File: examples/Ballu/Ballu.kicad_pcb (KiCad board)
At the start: 4 copper layers, 32.4 x 45.2 mm, 82 parts, among them J1 COM-15111, J2 B2B-PH-K, J4 AFC01-S30FCA-00, J5 PinHeader2.54 1x3, J6 PinHeader2.54 1x3, J7 B2B-PH-K, Q1 20V 3.1A 860mW 112m?@4.5V,2.8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, Q2 60V 115mA 200mW 7.5?@10V,500m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, Q3 30V 4A 44m?@10V,4.3A 1.4W 1.3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, SW1 SKRHABE010, SW2 5.1mm switch, U1 LDL1117S33R, U2 MCP73831T-2ACI/OT, U3 ESP32-S3-WROOM-1-N16R8, U4 PESD5V0X1BT, U5 LSM6DS3TR-C, U6 QMC5883L, U7 ER-OLED-0.96-1.1, U8 MAX98357AETE+T

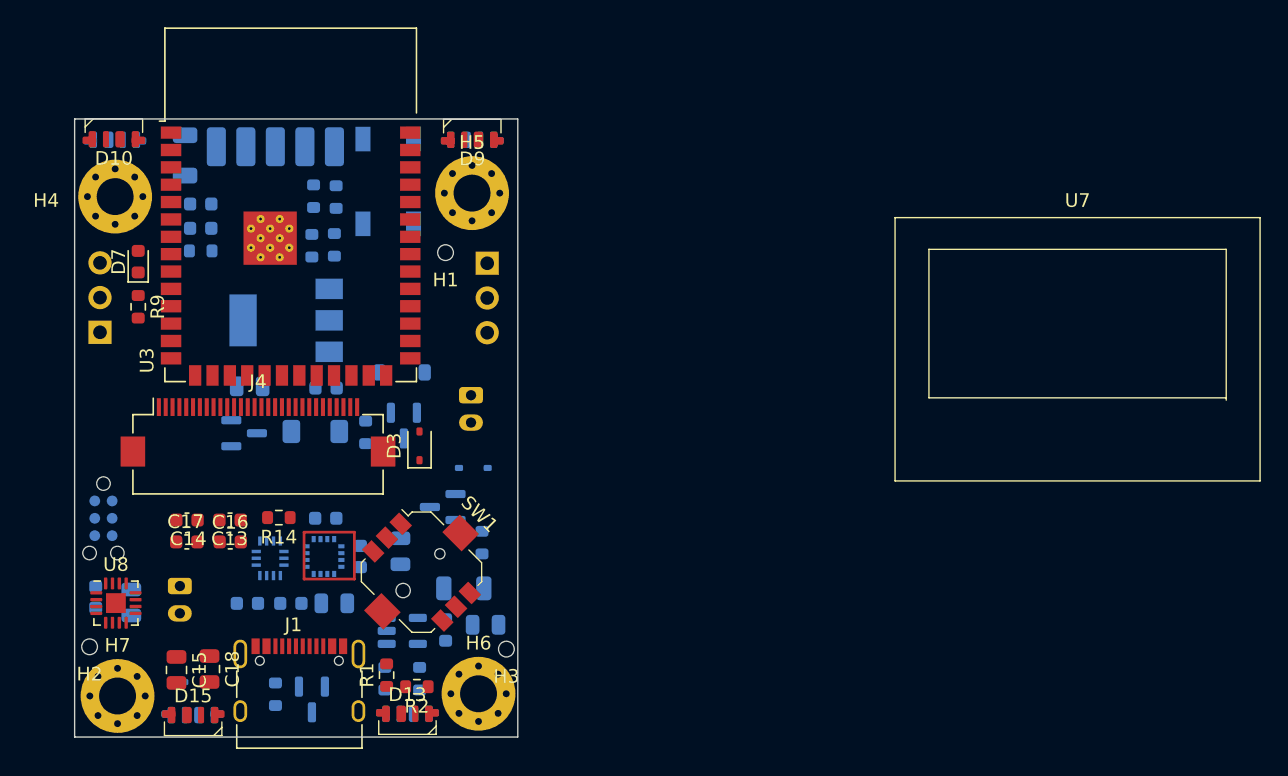
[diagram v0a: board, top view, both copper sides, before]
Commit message: Update: MCU pin assignments for better routing Update: PCB to be routed
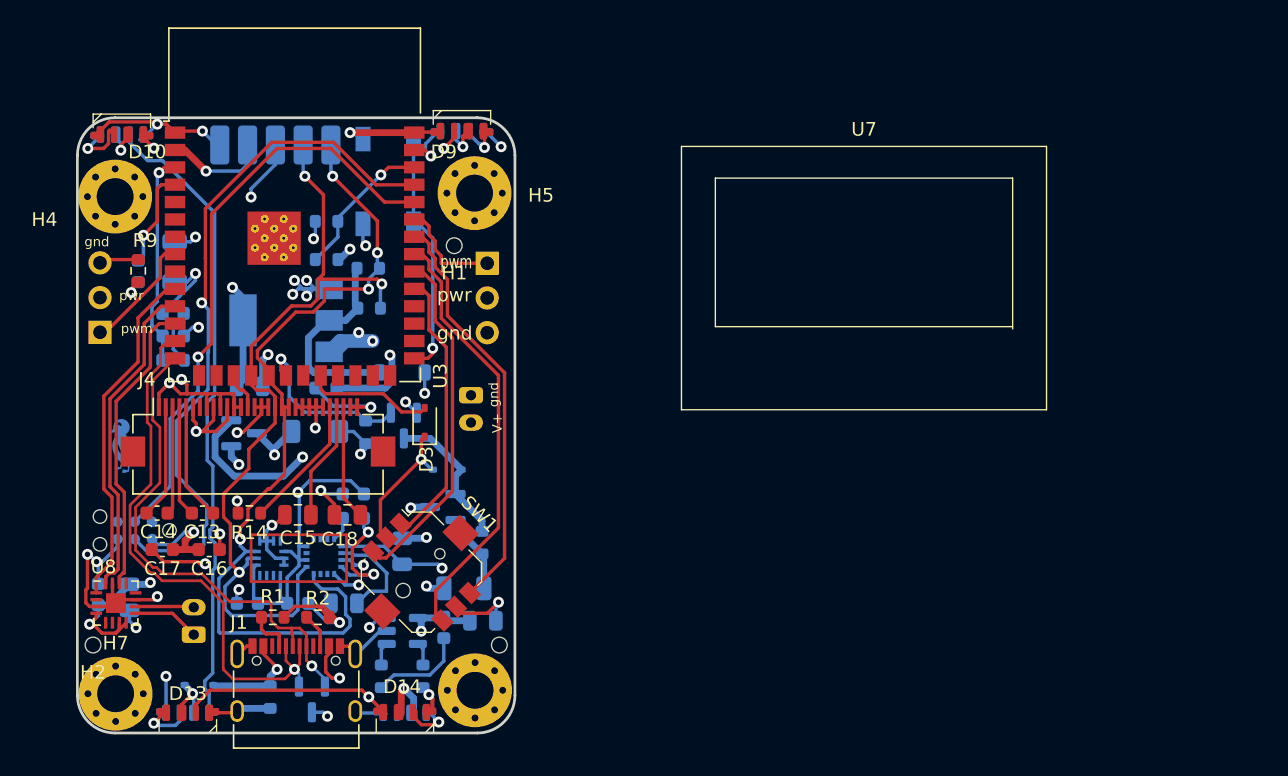
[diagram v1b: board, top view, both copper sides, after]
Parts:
- added svg2mod: G***, edg:Symbol_DucklingSolid, B.Cu at (103.0, 124.0)
- D14: moved to F.Cu
- D15, D7: moved to B.Cu
- moved U7 16.5 mm to (157.0, 109.8)
- moved D12 16.1 mm to (107.5, 144.1)
- moved D13 16.1 mm to (107.5, 144.1)
- moved D14 15.5 mm to (123.4, 144.1), turned to 0 degrees
- moved D15 15.5 mm to (123.4, 144.1), turned to 180 degrees
- moved C18 15.1 mm to (119.2, 129.0), turned to 180 degrees
- moved C15 14.4 mm to (115.6, 129.0), turned to 180 degrees
- moved R1 9.34 mm to (113.7, 136.5), turned to 180 degrees
- moved R10 9.14 mm to (120.8, 113.9), turned to 0 degrees
- moved R2 8.84 mm to (117.0, 136.5)
- moved R8 8.25 mm to (106.4, 117.7)
- moved C6 8.25 mm to (106.4, 114.3)
- moved C7 8.13 mm to (106.5, 116.0)
- moved C5 7.83 mm to (106.6, 110.5)
- moved R11 5.71 mm to (120.7, 111.0), turned to 0 degrees
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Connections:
- U3 pad 11: (no net) -> spk_drv.i2s.sck
- U3 pad 12: gate.btn_out -> spk_drv.i2s.ws
- U3 pad 15: i2c_chain_0.sda -> (no net)
- U3 pad 17: gate.dir_a -> oled.reset
- U3 pad 18: gate.dir_b -> i2c_chain_0.scl
- U3 pad 19: gate.dir_c -> i2c_chain_0.sda
- U3 pad 20: gate.dir_d -> gate.control
- U3 pad 21: gate.control -> (no net)
- U3 pad 22: spk_drv.i2s.sck -> gate.btn_out
- U3 pad 31: (no net) -> gate.dir_a
- U3 pad 32: (no net) -> gate.dir_c
- U3 pad 33: (no net) -> gate.dir_d
- U3 pad 34: (no net) -> gate.dir_b
- U3 pad 35: (no net) -> servo[1].pwm
- U3 pad 38: i2c_chain_0.scl -> batt_sense.output
- U3 pad 39: batt_sense.output -> npx_side.din
- U3 pad 5: oled.reset -> (no net)
- U3 pad 6: servo[0].pwm -> (no net)
- U3 pad 7: servo[1].pwm -> (no net)
- U3 pad 8: spk_drv.i2s.ws -> servo[0].pwm
- U3 pad 9: npx_side.din -> (no net)
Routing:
- net pwr: track 0.00 -> 169.4 mm, vias 0 -> 9
- net gnd: track 0.00 -> 155.4 mm, vias 0 -> 38
- net v3v3: track 0.00 -> 149.7 mm, vias 0 -> 9
- net i2c_chain_0.sda: track 0.00 -> 63.3 mm, vias 0 -> 4
- net i2c_chain_0.scl: track 0.00 -> 59.2 mm, vias 0 -> 3
- net mcu.program_uart_node.a_tx: track 0.00 -> 51.0 mm, vias 0 -> 1
- net npx_side.led[3].dout: track 0.00 -> 46.6 mm
- net vusb: track 0.00 -> 46.4 mm, vias 0 -> 4
- net mcu.program_uart_node.b_tx: track 0.00 -> 43.3 mm, vias 0 -> 1
- net gate.vbatt: track 0.00 -> 42.2 mm, vias 0 -> 3
- net usb_chain_0.d_N: track 0.00 -> 41.6 mm, vias 0 -> 1
- net usb_chain_0.d_P: track 0.00 -> 37.2 mm, vias 0 -> 1
- net gate.dir_d: track 0.00 -> 31.8 mm
- net gate.dir_b: track 0.00 -> 30.2 mm
- net gate.dir_c: track 0.00 -> 25.6 mm
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- added copper zone on In2.Cu, net gnd
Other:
- board size 32.4 x 45.2 mm -> 32 x 45 mm
- board text added: "3v3"
- board text added: "V+"
- board text added: "gnd"
- board text added: "pwm"
- board text added: "pwr"
- board text added: "scl"
- board text added: "sda"
- board text added: "vbatt"

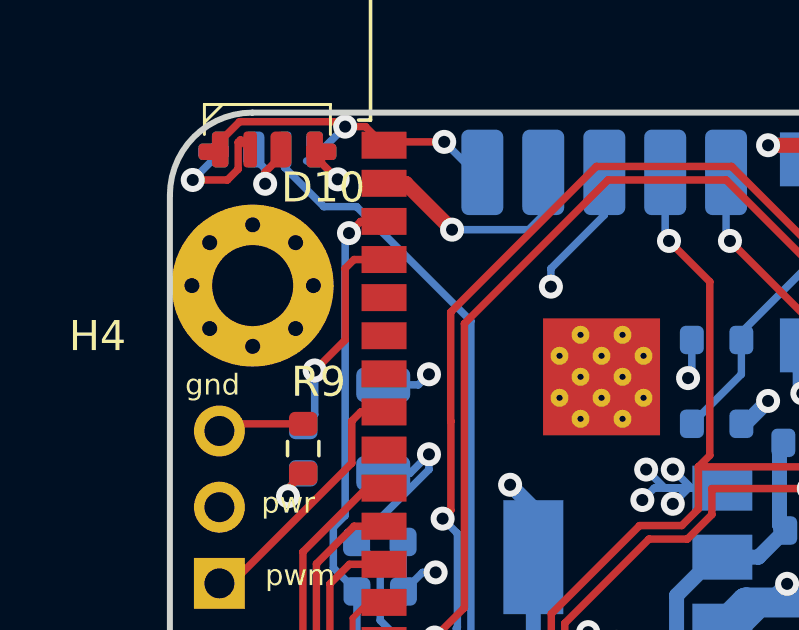
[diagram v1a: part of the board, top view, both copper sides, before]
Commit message: Fix: replace out of stock D2 diode (gaet.diode)
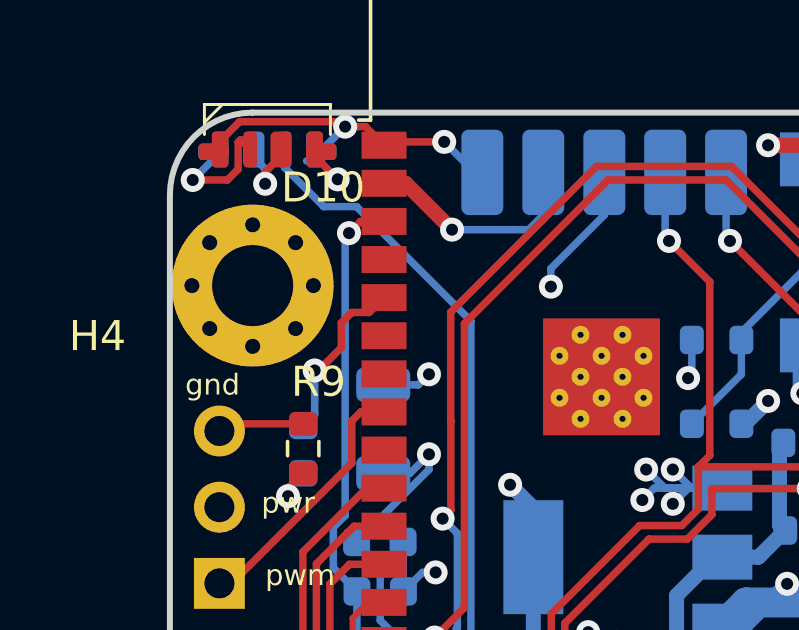
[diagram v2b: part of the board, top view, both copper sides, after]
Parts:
- D2: value 100nA@1V 25? Single 5.2V~6V 500mW 5.6V LL-34 Zener Diodes ROHS -> (none)
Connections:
- U3 pad 4: led.signal -> (no net)
- U3 pad 5: (no net) -> led.signal
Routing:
- net led.signal: track 7.25 -> 5.81 mm
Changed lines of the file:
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@@
     (pad "3" smd rect (at -8.75 -2.72) (size 1.5 0.9) (layers "F.Cu" "F.Paste" "F.Mask")
       (net 17 "mcu.program_en_node"))
-    (pad "4" smd rect (at -8.75 -1.45) (size 1.5 0.9) (layers "F.Cu" "F.Paste" "F.Mask")
+    (pad "4" smd rect (at -8.75 -1.45) (size 1.5 0.9) (layers "F.Cu" "F.Paste" "F.Mask"))
+    (pad "5" smd rect (at -8.75 -0.18) (size 1.5 0.9) (layers "F.Cu" "F.Paste" "F.Mask")
       (net 21 "led.signal"))
-    (pad "5" smd rect (at -8.75 -0.18) (size 1.5 0.9) (layers "F.Cu" "F.Paste" "F.Mask"))
     (pad "6" smd rect (at -8.75 1.09) (size 1.5 0.9) (layers "F.Cu" "F.Paste" "F.Mask"))
     (pad "7" smd rect (at -8.75 2.36) (size 1.5 0.9) (layers "F.Cu" "F.Paste" "F.Mask"))
@@
     (property "Sheetfile" "examples.components_lib.OrPowerGateDirSw")
     (property "Sheetname" "gate")
-    (property "edg_part" "ZMM5V6-M (ST(Semtech))")
+    (property "edg_part" "TCLLZ5V6TR (Tak Cheong)")
     (property "edg_path" "gate.prot.diode")
     (property "edg_refdes" "D2")
@@
         (effects (font (size 1 1) (thickness 0.15)) (justify mirror))
     )
-    (fp_text value "100nA@1V 25? Single 5.2V~6V 500mW 5.6V LL-34 Zener Diodes ROHS" (at 0 -2) (layer "B.Fab")
+    (fp_text value "" (at 0 -2) (layer "B.Fab")
         (effects (font (size 1 1) (thickness 0.15)) (justify mirror))
     )
@@
   (segment (start 121.666 138.870891) (end 122.065 138.471891) (width 0.25) (layer "B.Cu") (net 20))
   (segment (start 121.666 140.018) (end 121.666 138.870891) (width 0.25) (layer "B.Cu") (net 20))
-  (segment (start 105.579 104.887) (end 105.283 105.183) (width 0.25) (layer "F.Cu") (net 21))
-  (segment (start 105.283 107.569) (end 104.267 108.585) (width 0.25) (layer "F.Cu") (net 21))
-  (segment (start 105.283 105.183) (end 105.283 107.569) (width 0.25) (layer "F.Cu") (net 21))
-  (segment (start 106.579 104.887) (end 105.579 104.887) (width 0.25) (layer "F.Cu") (net 21))
+  (segment (start 106.579 106.157) (end 106.084 106.652) (width 0.25) (layer "F.Cu") (net 21))
+  (segment (start 106.084 106.652) (end 105.504 106.652) (width 0.25) (layer "F.Cu") (net 21))
+  (segment (start 105.504 106.652) (end 105.156 107) (width 0.25) (layer "F.Cu") (net 21))
+  (segment (start 105.156 107) (end 105.156 107.823) (width 0.25) (layer "F.Cu") (net 21))
+  (segment (start 104.394 108.585) (end 104.267 108.585) (width 0.25) (layer "F.Cu") (net 21))
+  (segment (start 105.156 107.823) (end 104.394 108.585) (width 0.25) (layer "F.Cu") (net 21))
   (via (at 104.267 108.585) (size 0.8) (drill 0.4) (layers "F.Cu" "B.Cu") (net 21))
   (segment (start 104.267 110.058) (end 103.886 110.439) (width 0.25) (layer "B.Cu") (net 21))

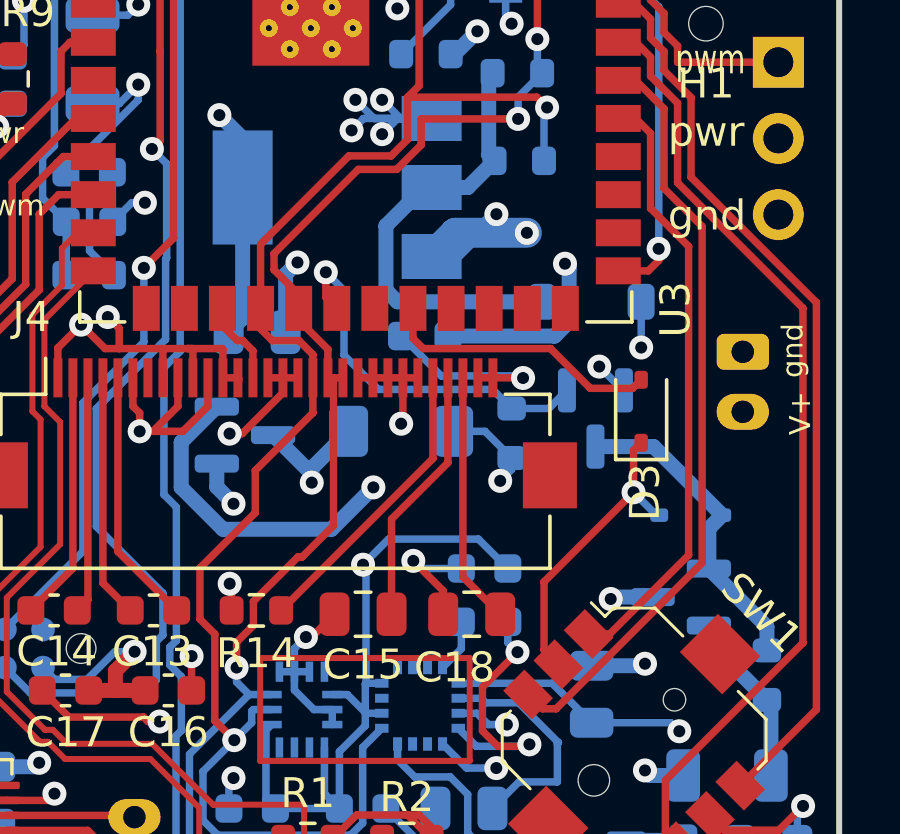
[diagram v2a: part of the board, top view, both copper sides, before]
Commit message: Add: FetPowerGate to be in the lib Update: FetPowerGate to have btn_in Update: Ballu to use the lib version of FetPowerGate with center as a power switch
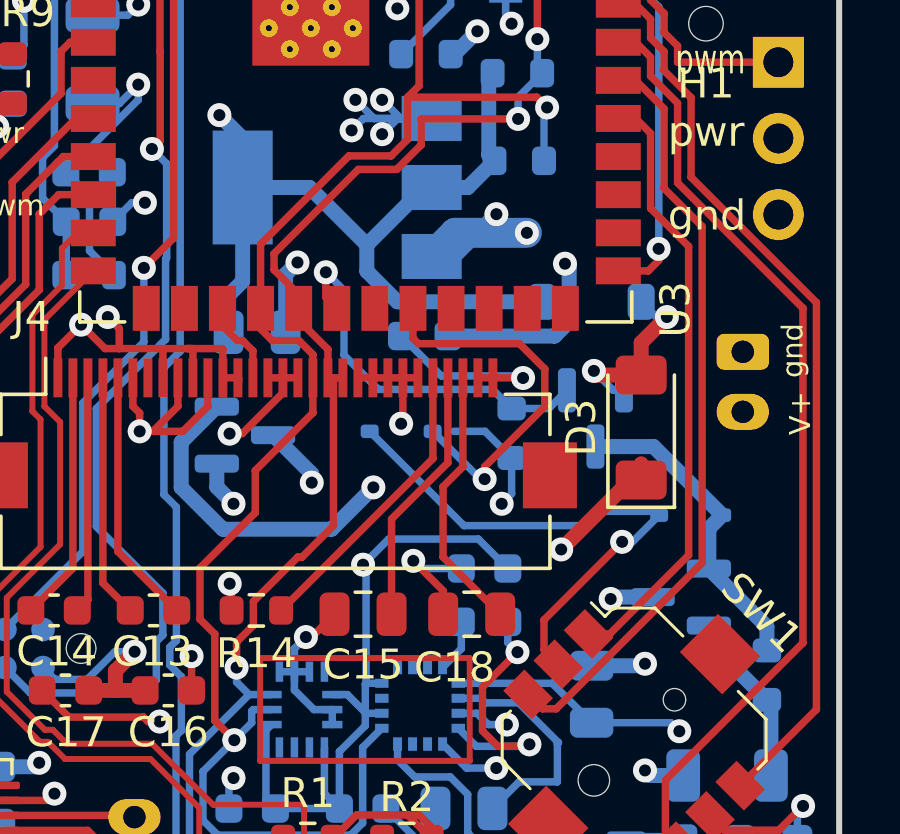
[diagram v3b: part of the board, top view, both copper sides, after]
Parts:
- D2: value (none) -> 30V 370mV@1mA 30mA SOD-323 Schottky Barrier Diodes (SBD) ROHS; footprint Diode_SMD:D_MiniMELF -> Diode_SMD:D_SOD-323
- D3: value 30V 370mV@1mA 30mA SOD-323 Schottky Barrier Diodes (SBD) ROHS -> (none); footprint Diode_SMD:D_SOD-323 -> Diode_SMD:D_MiniMELF
- moved D3 0.54 mm to (124.8, 122.8)
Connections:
- D1 pad 1: gate.gate_btn_out -> gate.dir.center
- D2 pad 1: gate.vbatt -> gate.dir.center
- D2 pad 2: gnd -> gate.btn_out
- D3 pad 1: gate.gate_btn_out -> gate.vbatt
- D3 pad 2: gate.btn_out -> gnd
- SW1 pad 2: gate.gate_btn_out -> gate.dir.center
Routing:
- net gate.dir.center: track 0.00 -> 18.2 mm, vias 0 -> 1
- net gate.gate_btn_out: track 10.1 -> 0.00 mm, vias 1 -> 0
- net v3v3: track 149.7 -> 155.2 mm
- net gnd: track 155.4 -> 159.7 mm
- net gate.btn_out: track 9.41 -> 12.7 mm, vias 0 -> 1
- net gate.vbatt: track 42.2 -> 43.6 mm, vias 3 -> 4
- net oled.device.vcc: track 8.39 -> 8.94 mm
